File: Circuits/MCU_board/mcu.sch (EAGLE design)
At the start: 31 parts, among them U1 TCA9548APWR, U2 USBLC6-2P6, U3 LD39050PU33R, U4 LSM9DS1, U5 STM32L452RECT6

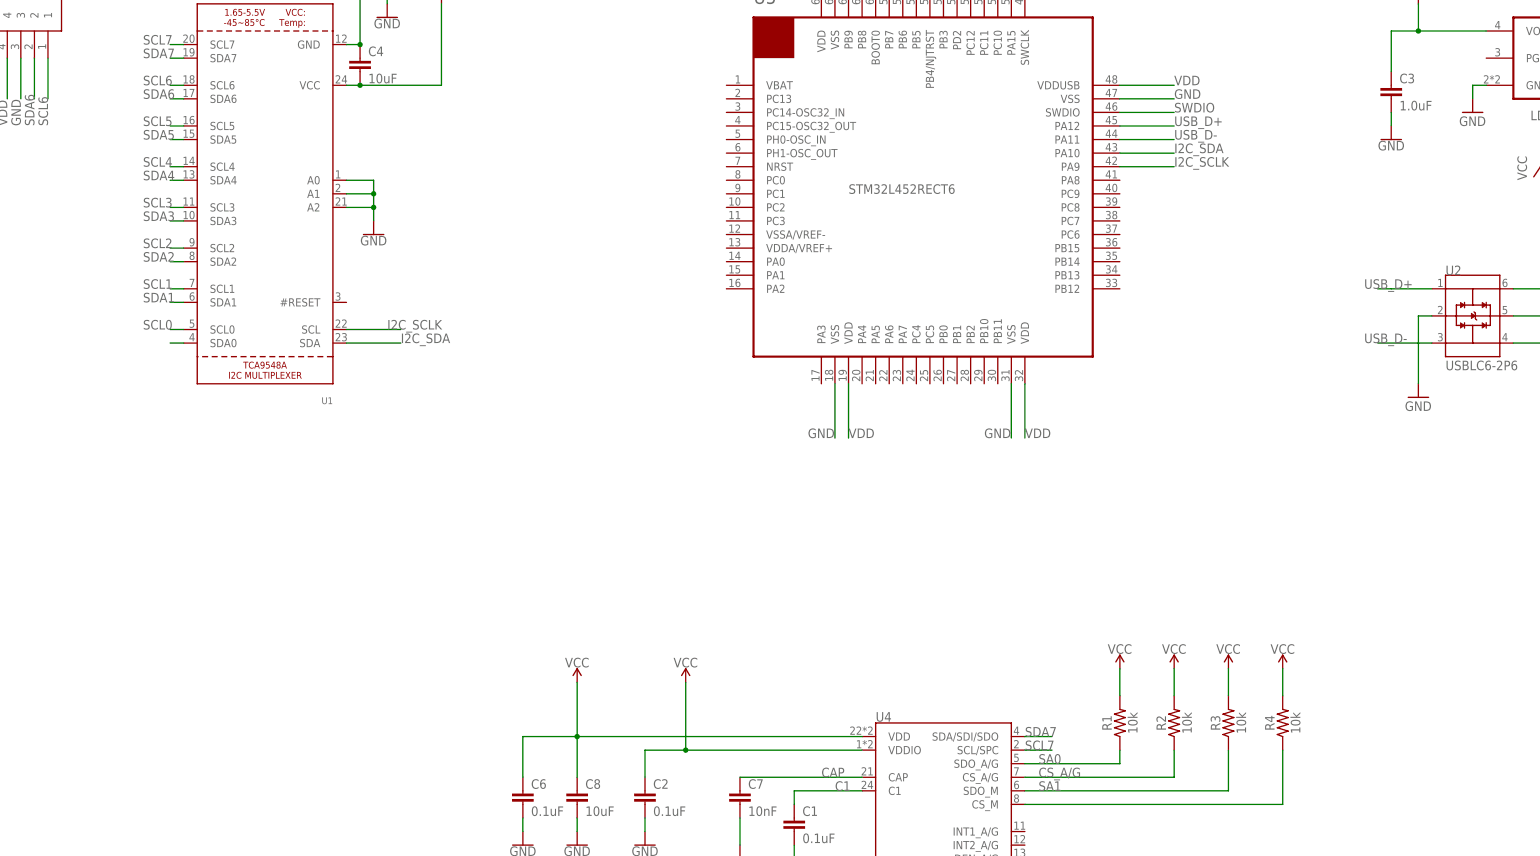
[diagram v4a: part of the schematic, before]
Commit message: Add SWD and reset to MCU board
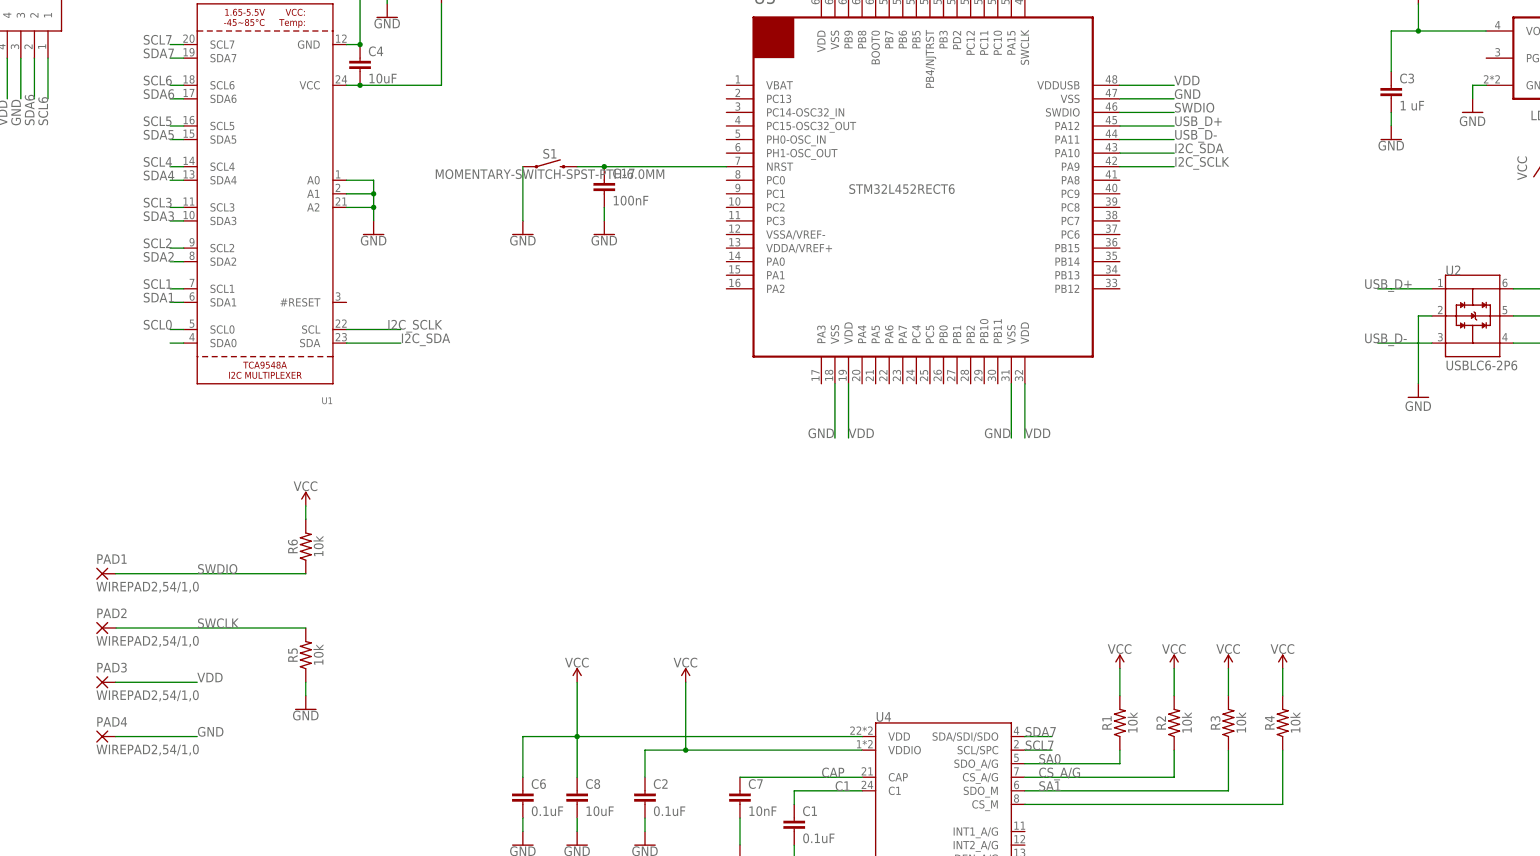
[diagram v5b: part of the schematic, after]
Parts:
- added C17: 100nF, SparkFun-Capacitors:0.18UF-0603-10V-10%
- added PAD1, PAD2, PAD3, PAD4: WIREPAD2,54/1,0, wirepad:WIREPAD2,54/1,0
- added R5, R6: 10k, SparkFun-Resistors:10KOHM-0603-1/10W-1%
- added S1: MOMENTARY-SWITCH-SPST-PTH-6.0MM, SparkFun-Switches:MOMENTARY-SWITCH-SPST-PTH-6.0MM
- C3: value 1.0uF -> 1 uF; device SparkFun-Capacitors:1.0UF-0402-16V-10% -> SparkFun-Capacitors:0.18UF-0603-10V-10%
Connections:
- new net N$4: C17.1, S1.2, U5.NRST
- net GND: now also C17.2, PAD4.P, R5.1, S1.1
- net SWCLK: now also PAD2.P, R5.2
- net SWDIO: now also PAD1.P, R6.1
- net VCC: now also R6.2
- net VDD: now also PAD3.P

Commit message: Add I2C mux reset GPIO
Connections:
- new net I2C_MUX_RST: U1.#RESET, U5.PA6
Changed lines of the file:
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@@
 <pinref part="U5" gate="G$1" pin="VSS@18"/>
 <wire x1="71.12" y1="50.8" x2="71.12" y2="40.64" width="0.1524" layer="91"/>
-<label x="66.04" y="40.64" size="1.778" layer="95"/>
+<label x="71.12" y="35.56" size="1.778" layer="95" rot="R90"/>
 </segment>
 <segment>
@@
 <pinref part="U5" gate="G$1" pin="VDD@19"/>
 <wire x1="73.66" y1="50.8" x2="73.66" y2="40.64" width="0.1524" layer="91"/>
-<label x="73.66" y="40.64" size="1.778" layer="95"/>
+<label x="73.66" y="35.56" size="1.778" layer="95" rot="R90"/>
 </segment>
 <segment>
@@
 </segment>
 </net>
+<net name="I2C_MUX_RST" class="0">
+<segment>
+<pinref part="U5" gate="G$1" pin="PA6"/>
+<wire x1="81.28" y1="50.8" x2="81.28" y2="40.64" width="0.1524" layer="91"/>
+<label x="81.28" y="25.4" size="1.778" layer="95" rot="R90"/>
+</segment>
+<segment>
+<pinref part="U1" gate="G$1" pin="#RESET"/>
+<wire x1="-20.32" y1="66.04" x2="-10.16" y2="66.04" width="0.1524" layer="91"/>
+<label x="-10.16" y="66.04" size="1.778" layer="95"/>
+</segment>
+</net>

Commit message: set I2C lines for IMU on mcu board
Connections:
- net SCL6: now also U4.SCL/SPC
- net SCL7: no longer U4.SCL/SPC
- net SDA6: now also U4.SDA/SDI/SDO
- net SDA7: no longer U4.SDA/SDI/SDO
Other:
- moved on the sheet: C1, C10, C11, C12, C13, C14, C15, C16, C2, C6, C7, C8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

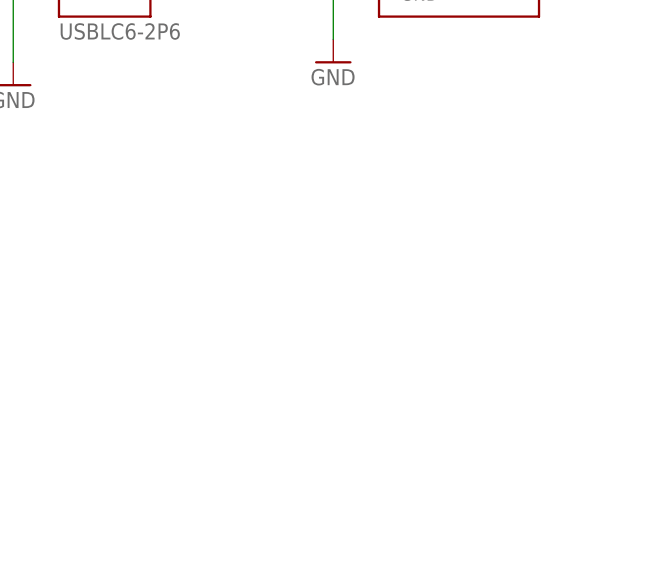
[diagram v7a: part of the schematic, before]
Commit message: Added LDO part in schematic
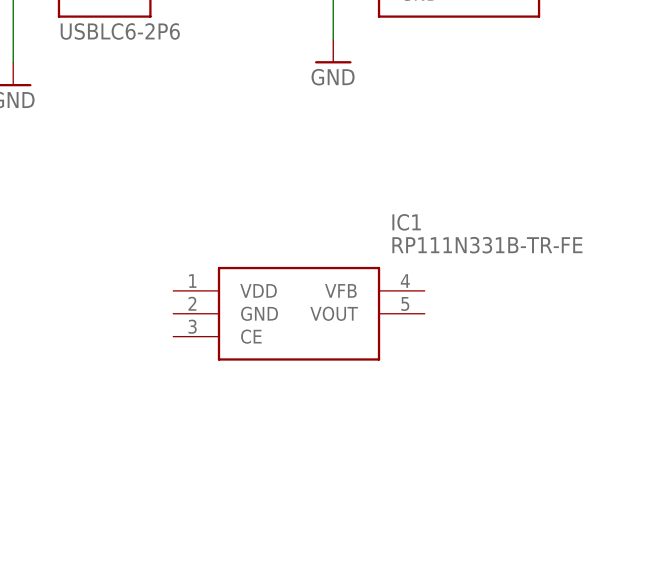
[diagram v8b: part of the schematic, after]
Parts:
- added IC1: RP111N331B-TR-FE, SamacSys_Parts:RP111N331B-TR-FE
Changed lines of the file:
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@@
 <?xml version="1.0" encoding="utf-8"?>
 <!DOCTYPE eagle SYSTEM "eagle.dtd">
-<eagle version="9.3.2">
+<eagle version="9.4.2">
 <drawing>
 <settings>
@@
 <part name="C17" library="SparkFun-Capacitors" deviceset="0.18UF" device="-0603-10V-10%" value="100nF"/>
 <part name="C3" library="SparkFun-Capacitors" deviceset="0.18UF" device="-0603-10V-10%" value="1 uF"/>
+<part name="IC1" library="SamacSys_Parts" deviceset="RP111N331B-TR-FE" device=""/>
 </parts>
 <sheets>
@@
 <attribute name="VALUE" x="176.784" y="101.981" size="1.778" layer="96" font="vector"/>
 </instance>
+<instance part="IC1" gate="G$1" x="198.12" y="25.4" smashed="yes">
+<attribute name="NAME" x="222.25" y="33.02" size="1.778" layer="95" align="center-left"/>
+<attribute name="VALUE" x="222.25" y="30.48" size="1.778" layer="96" align="center-left"/>
+</instance>
 </instances>
